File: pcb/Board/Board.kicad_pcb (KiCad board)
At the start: 2 copper layers, 145.5 x 73.3 mm, 66 parts, among them J1 Conn_01x04_Female, J2 TRRS_SJ1-42514, K00 KEYSW, K01 KEYSW, K02 KEYSW, K03 KEYSW, K04 KEYSW, K05 KEYSW, K10 KEYSW, K11 KEYSW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

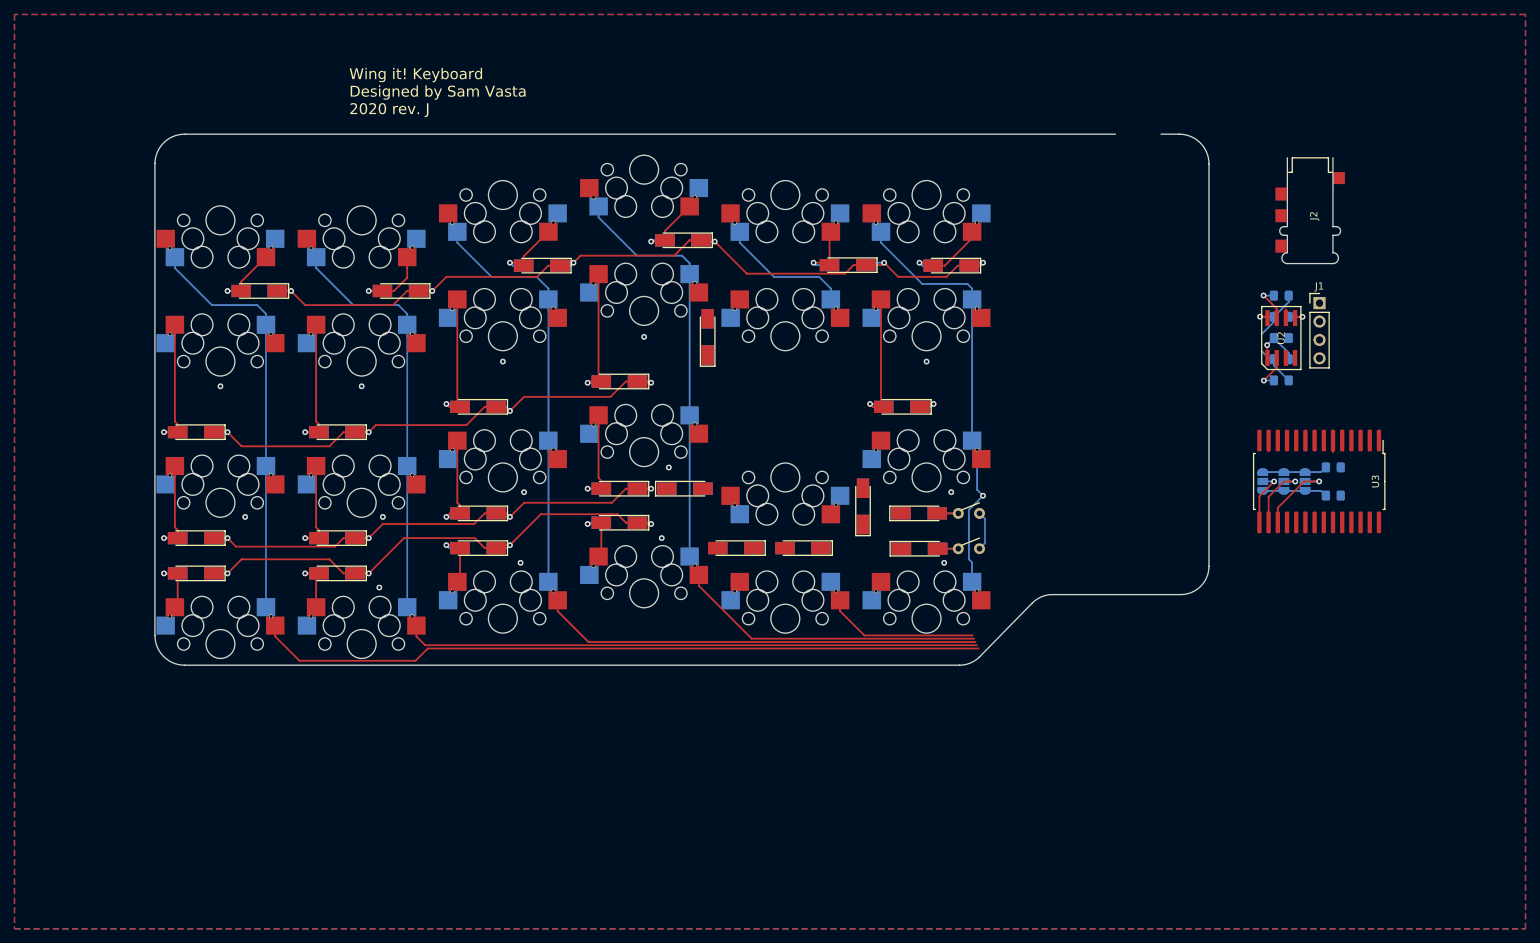
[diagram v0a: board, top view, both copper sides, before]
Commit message: Fixed DRC errors
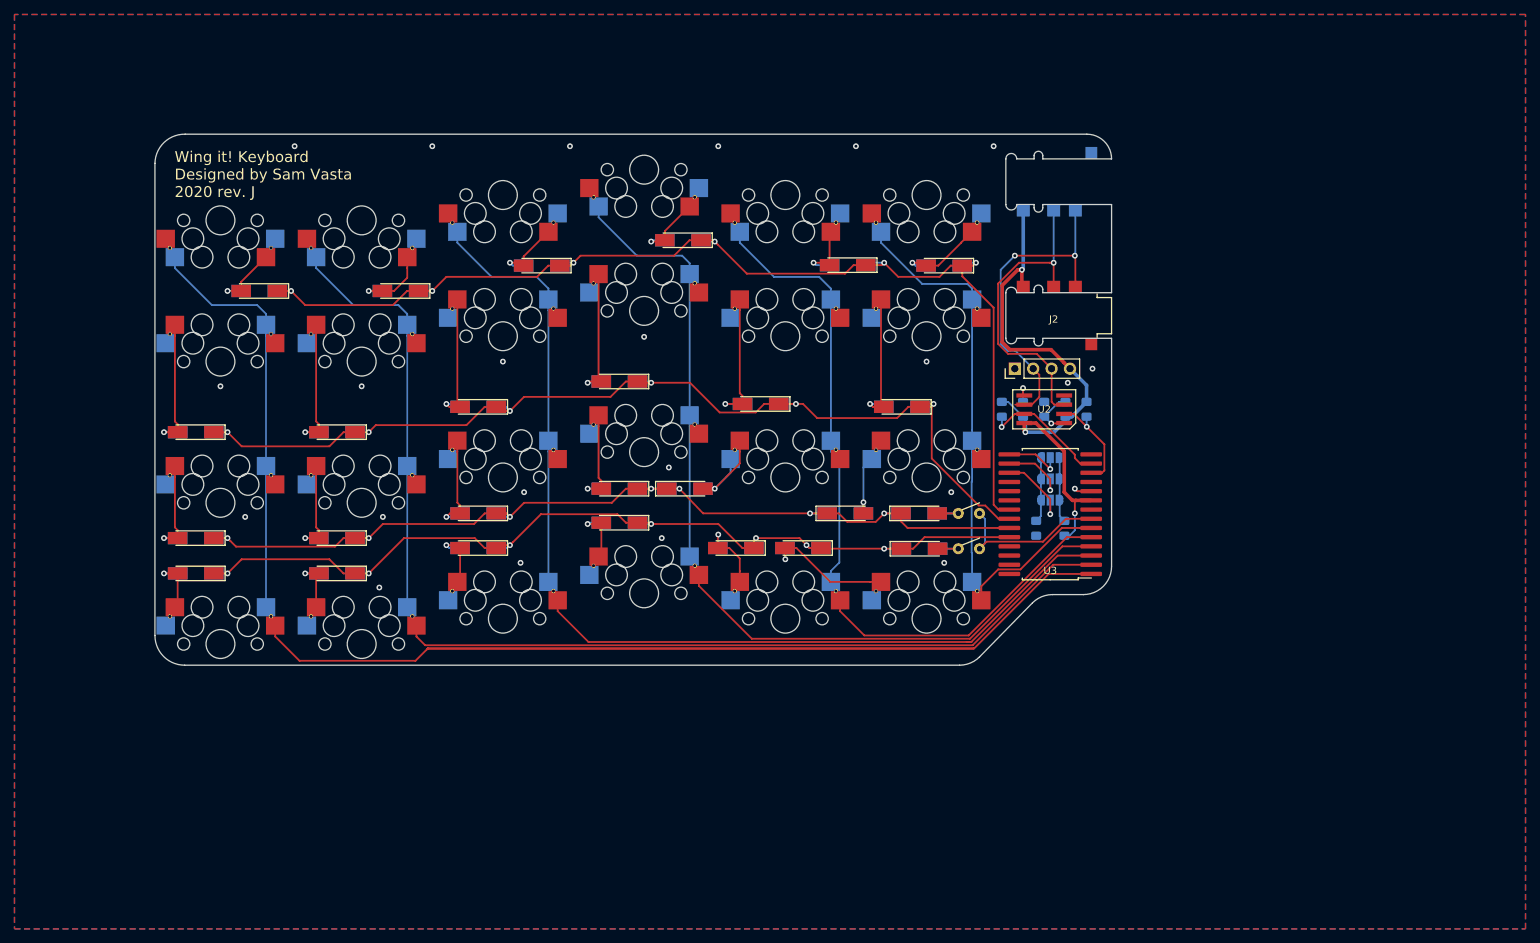
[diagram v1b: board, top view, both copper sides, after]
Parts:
- added G***: LOGO, SVastaCustomParts:wing_it_400dpi, B.Cu at (213.3, 48.9)
- added J2: TRRS_SJ1-42514, SVastaCustomParts:3.5mm_Cut_out, F.Cu at (322.0, 67.9)
- J2: moved to B.Cu
- moved J1 43.0 mm to (316.6, 75.2), turned to 90 degrees
- moved R203 41.7 mm to (314.8, 80.8), turned to 90 degrees
- moved R302 41.3 mm to (319.5, 97.3), turned to 270 degrees
- moved R301 38.1 mm to (323.4, 97.3), turned to 270 degrees
- moved R204 37.9 mm to (317.7, 80.8), turned to 270 degrees
- moved U3 37.4 mm to (321.5, 95.3), turned to 180 degrees
- moved J2 35.8 mm to (322.0, 49.4), turned to 180 degrees
- moved 4 35.3 mm to (321.5, 93.4), turned to 180 degrees
- moved C201 34.2 mm to (320.7, 80.8), turned to 90 degrees
- moved U2 34.2 mm to (320.7, 80.8), turned to 90 degrees
- moved 2 32.3 mm to (321.5, 90.5), turned to 180 degrees
- moved R201 30.6 mm to (323.6, 80.8), turned to 90 degrees
- moved 1 29.5 mm to (321.5, 87.5), turned to 180 degrees
- moved R202 27.2 mm to (326.5, 80.8), turned to 90 degrees
- moved D14 11.8 mm to (281.5, 80.1), turned to 180 degrees
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- renumbered JP0 to 1, JP1 to 2, JP2 to 4
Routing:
- net /SwitchMatrix/Col0: track 170.9 -> 266.2 mm
- net /SwitchMatrix/Row1: track 77.4 -> 143.4 mm, vias 5 -> 6
- net /SwitchMatrix/Col4: track 48.6 -> 113.6 mm
- net VCC: track 15.7 -> 79.3 mm, vias 1 -> 3
- net /SwitchMatrix/Row2: track 72.3 -> 134.3 mm, vias 4 -> 7
- net /SwitchMatrix/Row3: track 75.9 -> 135.2 mm, vias 4 -> 7
- net SDA: track 1.24 -> 45.8 mm, vias 0 -> 2
- net SCL: track 0.00 -> 43.0 mm, vias 0 -> 1
- net /SwitchMatrix/Row0: track 119.6 -> 155.9 mm
- net /SwitchMatrix/Col2: track 130.5 -> 152.0 mm
- net /SwitchMatrix/Col3: track 112.0 -> 133.5 mm
- net Net-(D24-Pad2): track 0.00 -> 21.0 mm, vias 0 -> 1
- net /SwitchMatrix/Col5: track 70.6 -> 91.5 mm, vias 1 -> 0
- net /SwitchMatrix/Col1: track 148.9 -> 169.2 mm
- net Net-(D14-Pad2): track 3.07 -> 22.4 mm, vias 0 -> 1
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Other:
- board size 145.5 x 73.3 mm -> 132.1 x 73.3 mm
- board text added: "GND"
- board text added: "SCL"
- board text added: "SDA"
- board text added: "VCC"

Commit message: updaaaaaaates
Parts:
- added J3: Conn_01x12_Female, Connector_PinHeader_2.54mm:PinHeader_1x12_P2.54mm_Vertical, F.Cu at (280.5, 80.6)
- moved D15 5.76 mm to (301.0, 74.7)
- moved D14 5.36 mm to (281.5, 74.7)
- moved D10 3.90 mm to (203.5, 80.1)
- moved D11 3.90 mm to (223.0, 80.1)
- moved D12 3.90 mm to (242.5, 76.6)
- moved D13 3.90 mm to (262.0, 73.1)
- renumbered 1 to JP0, 2 to JP1, 4 to JP2
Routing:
- net /SwitchMatrix/Col0: track 266.2 -> 339.5 mm
- net /SwitchMatrix/Col1: track 169.2 -> 226.8 mm
- net /SwitchMatrix/Col2: track 152.0 -> 191.1 mm
- net /SwitchMatrix/Col6: track 22.6 -> 51.9 mm
- net /SwitchMatrix/Col5: track 91.5 -> 118.9 mm
- net /SwitchMatrix/Row0: track 155.9 -> 181.8 mm
- net /SwitchMatrix/Row3: track 135.2 -> 159.2 mm
- net /SwitchMatrix/Col3: track 133.5 -> 151.6 mm
- net /SwitchMatrix/Row2: track 134.3 -> 151.0 mm
- net Net-(D15-Pad2): track 22.2 -> 13.9 mm
- net Net-(D14-Pad2): track 22.4 -> 16.1 mm
- net Net-(D11-Pad2): track 21.8 -> 17.9 mm
- net Net-(D10-Pad2): track 21.8 -> 17.9 mm
- net Net-(D13-Pad2): track 22.0 -> 18.1 mm
- net Net-(D12-Pad2): track 22.2 -> 18.3 mm
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- removed copper zone on F.Cu, net GND
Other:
- board text added: "1"
- board text added: "2"
- board text added: "4"
- board text added: "C0"
- board text added: "C1"
- board text added: "C2"
- board text added: "C3"
- board text added: "C4"
- board text added: "C5"
- board text added: "C6"
- board text added: "C7"
- board text added: "R0"
- board text added: "R1"
- board text added: "R2"
- board text added: "R3"
- board text added: "Wing it! Keyboard Designed by Sam Vasta 2020 rev. K"
- board text removed: "Wing it! Keyboard Designed by Sam Vasta 2020 rev. J"
